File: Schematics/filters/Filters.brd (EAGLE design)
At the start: 100.6 x 50.8 mm, 102 parts, among them IC1 NE5532N, IC2 NE5532N, IC3 NE5532N, IC4 NE5532N, IC5 NE5532N, IC6 NE5532N, IC7 NE5532N, J1 3_PIN_AMPCONN, J2 3_PIN_AMPCONN, J3 3_PIN_AMPCONN

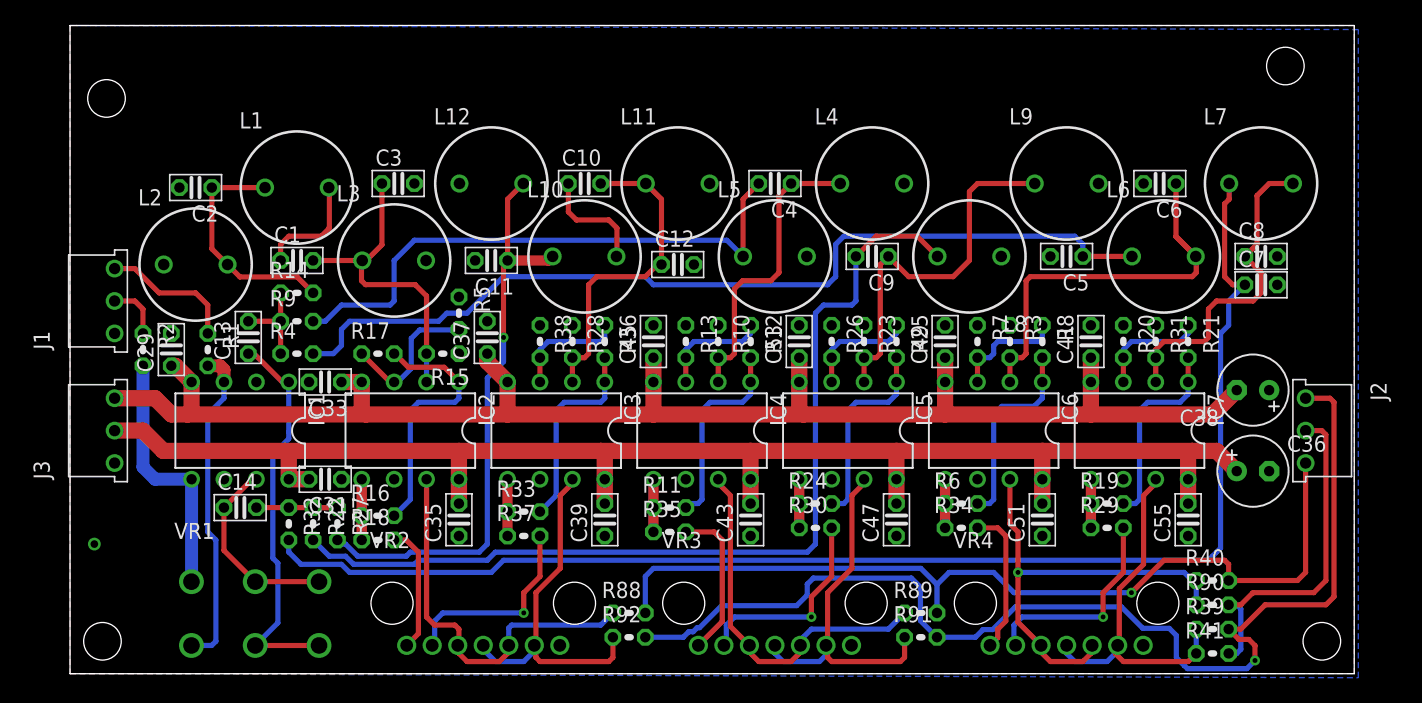
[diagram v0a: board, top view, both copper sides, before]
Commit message: Schematic update
Fixed silkscreen, board outline and a few components
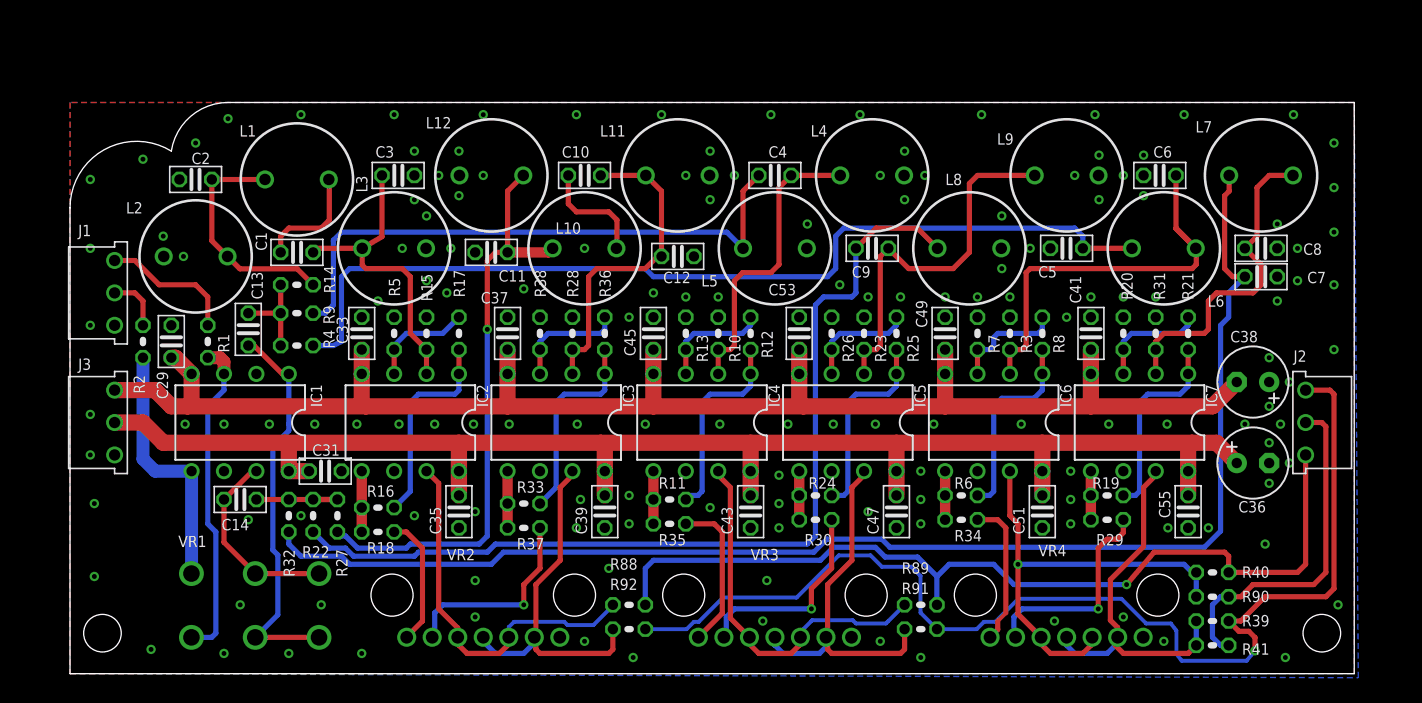
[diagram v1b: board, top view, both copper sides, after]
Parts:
- moved R17 6.55 mm to (30.5, 26.7), turned to 270 degrees
- moved R5 5.32 mm to (25.4, 26.7)
- moved C33 4.76 mm to (22.9, 26.7), turned to 90 degrees
- moved R15 2.03 mm to (27.9, 26.7), turned to 270 degrees
- moved C37 1.62 mm to (34.3, 26.7)
- moved L3 0.95 mm to (25.4, 33.3)
- moved C1 0.64 mm to (17.8, 33.0)
- moved C10 0.64 mm to (40.3, 39.1)
- moved C11 0.64 mm to (33.0, 33.0)
- moved C3 0.64 mm to (25.7, 39.1)
- moved C4 0.64 mm to (55.2, 39.1)
- moved C6 0.64 mm to (85.4, 39.1)
- moved L11 0.64 mm to (47.6, 39.1)
- moved L12 0.64 mm to (33.0, 39.1)
- moved L4 0.64 mm to (62.9, 39.1)
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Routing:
- net N$15: track 20.3 -> 16.2 mm
- net N$27: track 11.6 -> 8.22 mm
- net N$12: track 72.0 -> 74.1 mm
- net N$13: track 44.9 -> 46.1 mm
- net N$10: track 70.0 -> 70.9 mm
- net N$21: track 30.8 -> 29.8 mm
- net N$38: track 88.6 -> 89.3 mm
- net -12V: track 121.6 -> 121.0 mm
- net N$64: track 29.4 -> 30.1 mm
- net N$34: track 45.8 -> 46.3 mm
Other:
- board size 100.6 x 50.8 mm -> 100.6 x 44.8 mm
